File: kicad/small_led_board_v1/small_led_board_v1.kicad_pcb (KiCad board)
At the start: 2 copper layers, 132 x 102.9 mm, 107 parts, among them J1 TO FPGA, J2 +5V IN, Q1 IRLZ44N, Q10 IRF4905, Q11 IRF4905, Q12 IRF4905, Q13 IRF4905, Q14 IRF4905, Q15 IRLZ44N, Q16 IRLZ44N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

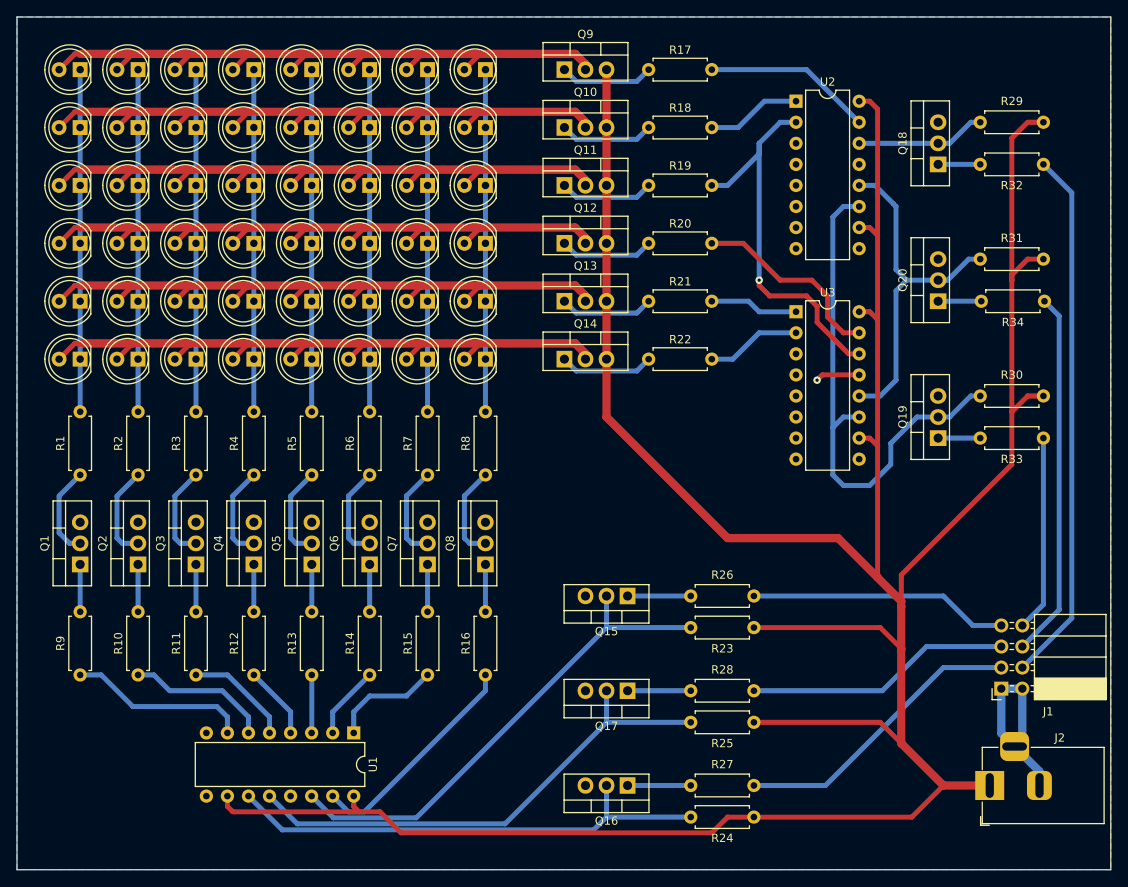
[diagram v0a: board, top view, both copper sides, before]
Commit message: kicad: migration complete to 9.0, small led boards both done
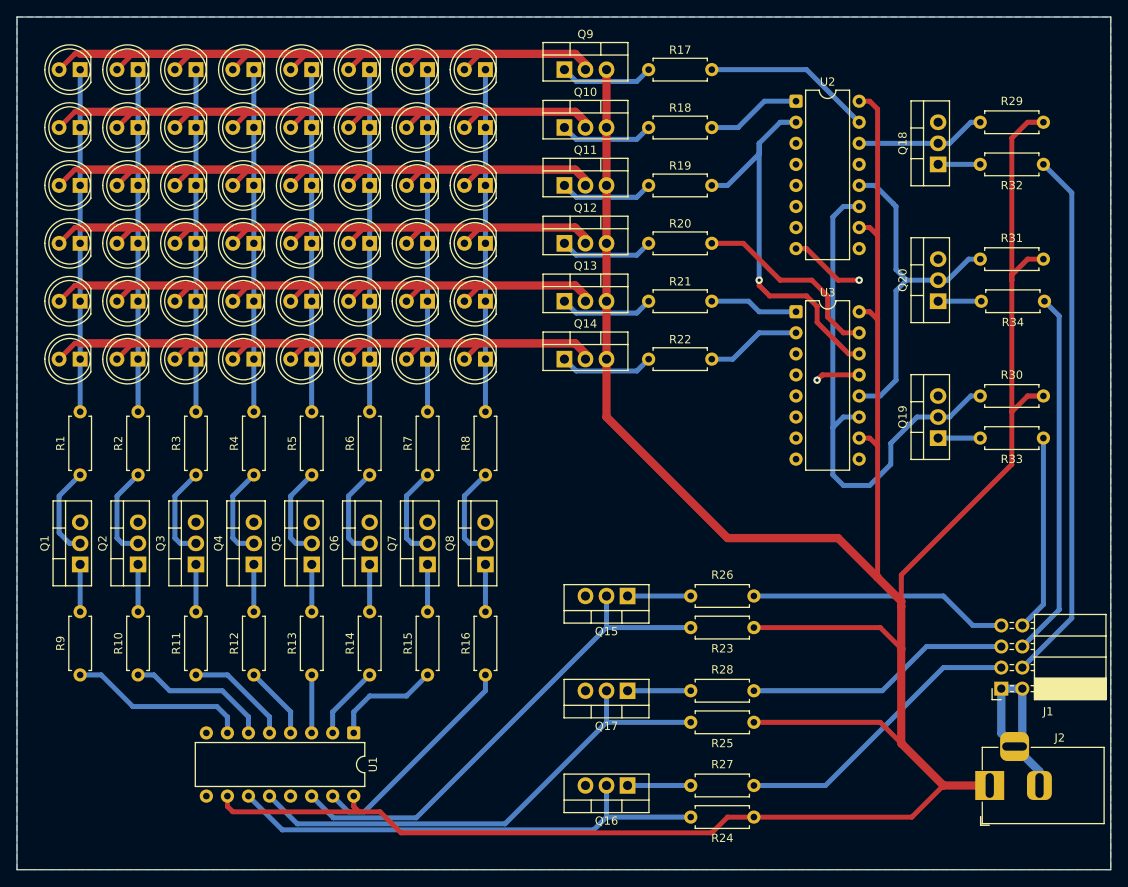
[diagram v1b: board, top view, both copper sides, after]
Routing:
- net GND: track 28.8 -> 38.0 mm, vias 1 -> 2
